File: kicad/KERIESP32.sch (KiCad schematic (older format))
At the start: 30 parts, among them P1 GPIO_0-19, P2 GPIO_21-27, P3 GPIO_32-39, P4 SD_DETECT, P5 USB_Micro_B, P6 GND, P7 Power, SW1 GPIO0, SW2 RESET, U1 ESP-WROOM-32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

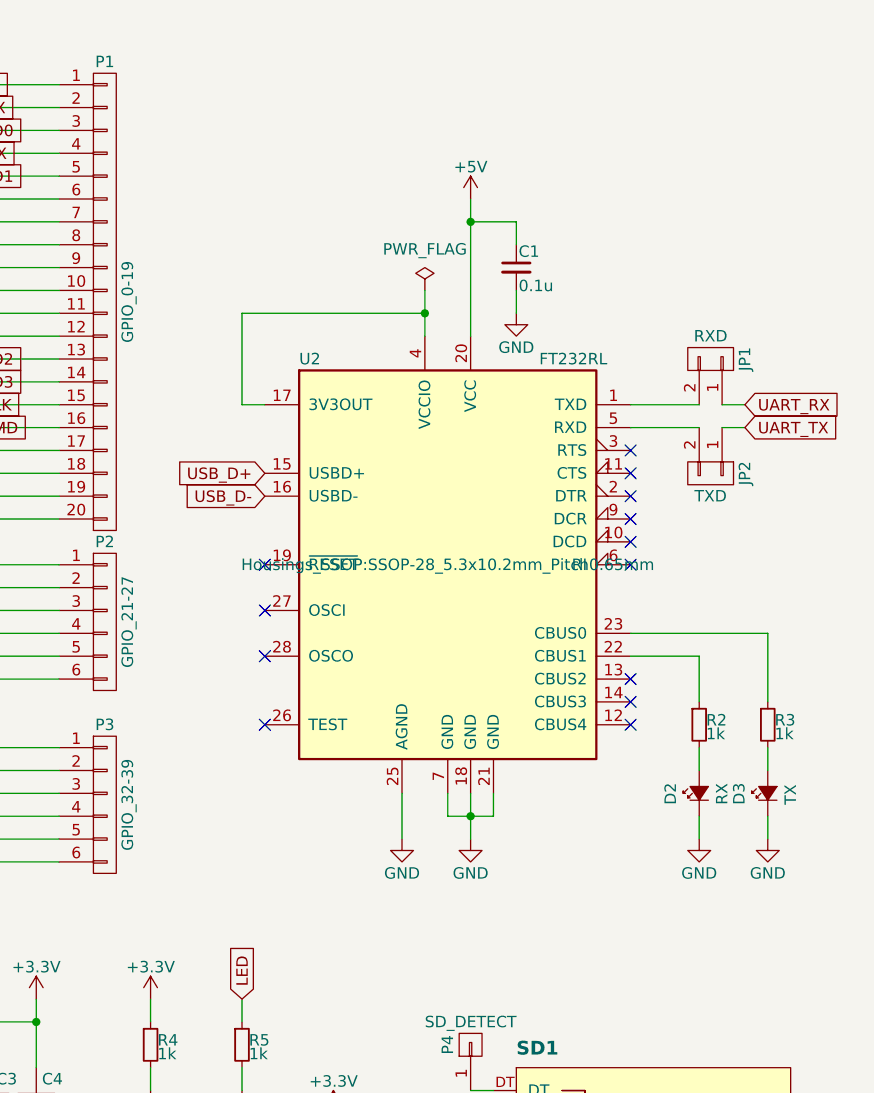
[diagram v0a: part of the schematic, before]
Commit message: 部品表，回路図PDFを生成
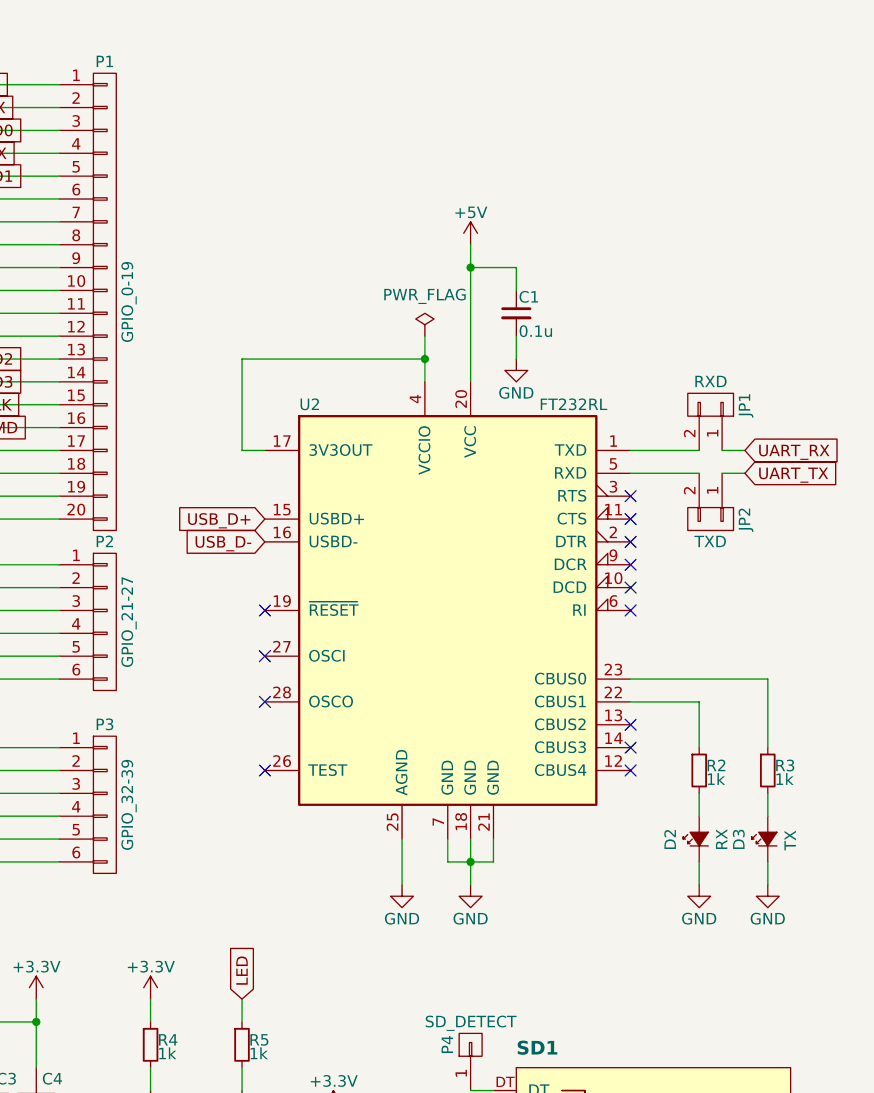
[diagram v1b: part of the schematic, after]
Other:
- moved on the sheet: C1, D2, D3, JP1, JP2, R2, R3, U2

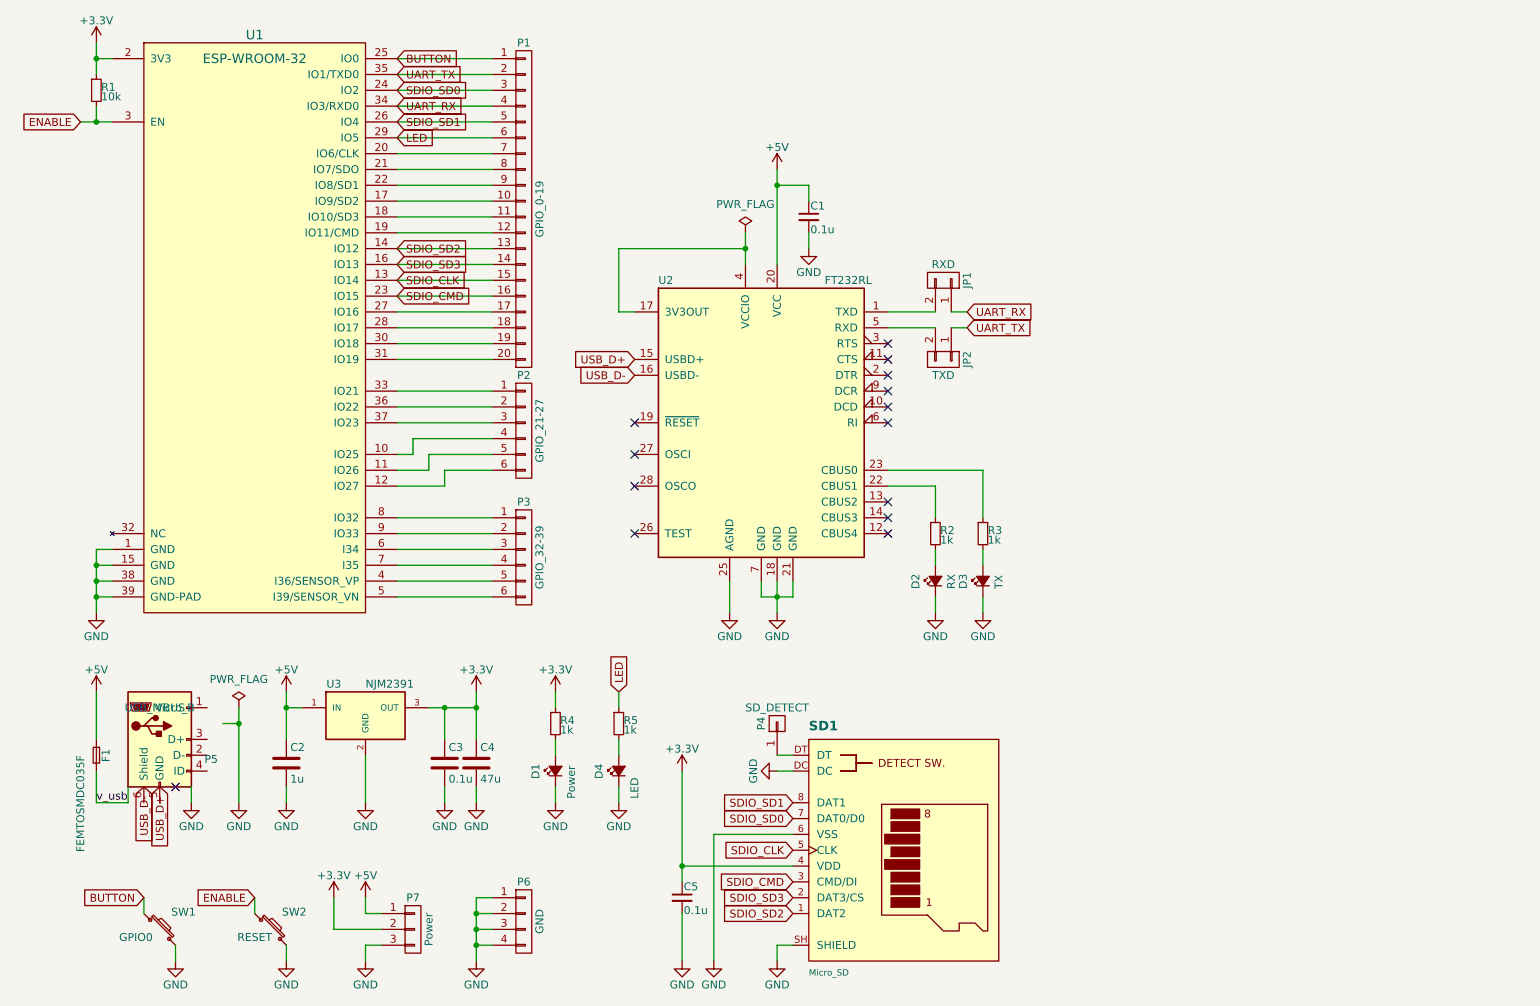
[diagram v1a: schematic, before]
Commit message: 台形型変換基板を設計
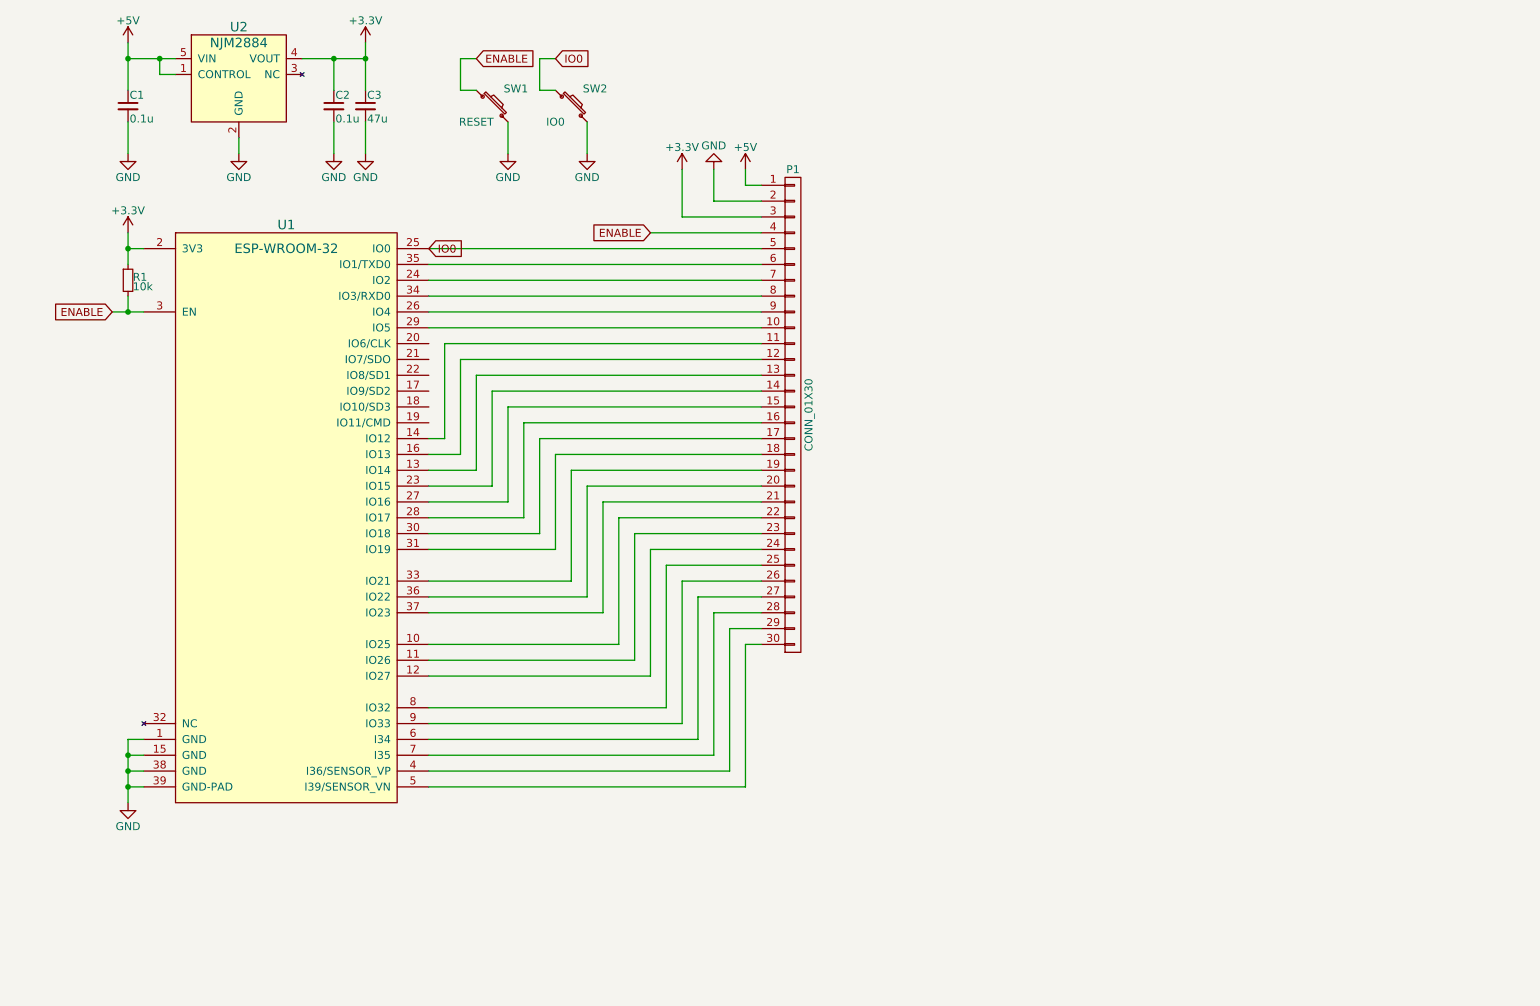
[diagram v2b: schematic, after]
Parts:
- removed C2: 1u, Capacitors_SMD:C_0603, symbol C
- removed C3: 0.1u, Capacitors_SMD:C_0603, symbol C
- removed C4: 47u, Capacitors_SMD:C_1206, symbol C
- removed C5: 0.1u, Capacitors_SMD:C_0603, symbol C_Small
- removed D1: Power, LEDs:LED_0603, symbol Led_Small
- removed D2: RX, LEDs:LED_0603, symbol Led_Small
- removed D3: TX, LEDs:LED_0603, symbol Led_Small
- removed D4: LED, LEDs:LED_0603, symbol Led_Small
- removed F1: FEMTOSMDC035F, Resistors_SMD:R_0603, symbol F_Small
- removed JP1: RXD, Pin_Headers:Pin_Header_Straight_2x01, symbol CONN_01X02
- removed JP2: TXD, Pin_Headers:Pin_Header_Straight_2x01, symbol CONN_01X02
- removed P1: GPIO_0-19, Socket_Strips:Socket_Strip_Straight_1x20, symbol CONN_01X20
- removed P2: GPIO_21-27, Socket_Strips:Socket_Strip_Straight_1x06, symbol CONN_01X06
- removed P3: GPIO_32-39, Socket_Strips:Socket_Strip_Straight_1x06, symbol CONN_01X06
- removed P4: SD_DETECT, Socket_Strips:Socket_Strip_Straight_1x01, symbol CONN_01X01
- removed P5: USB_Micro_B, kerikun11:USB_Micro_B_smd, symbol USB_OTG
- removed P6: GND, Socket_Strips:Socket_Strip_Straight_1x04, symbol CONN_01X04
- removed P7: Power, Socket_Strips:Socket_Strip_Straight_1x03, symbol CONN_01X03
- removed R2, R3, R4, R5: 1k, Resistors_SMD:R_0603, symbol R_Small
- removed SD1: Micro_SD, conn-io:HIROSE-MICROSD-DM3AT-SF, symbol Micro_SD
- removed U2: FT232RL, Housings_SSOP:SSOP-28_5.3x10.2mm_Pitch0.65mm, symbol FT232RL
- removed U3: NJM2391, TO_SOT_Packages_SMD:TO-252-2Lead, symbol LM7805CT
- added C2: 0.1u, Capacitors_SMD:C_0603, symbol C_Small
- added C3: 47u, Capacitors_SMD:C_1206, symbol C_Small
- added P1: CONN_01X30, Pin_Headers:Pin_Header_Straight_1x30, symbol CONN_01X30
- added U2: NJM2884, TO_SOT_Packages_SMD:SOT89-5_Housing, symbol NJM2884
- SW1: value GPIO0 -> RESET; footprint Buttons_Switches_SMD:SW_SPST_KMR2 -> kerikun11:SW_PUSH
- SW2: value RESET -> IO0; footprint Buttons_Switches_SMD:SW_SPST_KMR2 -> kerikun11:SW_PUSH
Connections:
- net +3V3: now also C2.1, C3.1, P1.3 (P3), U2.4 (VOUT)
- net +5V: now also P1.1 (P1), U2.1 (CONTROL), U2.5 (VIN)
- net ENABLE: now also SW1.1, P1.4 (P4); no longer SW2.1
- net GND: now also C2.2, C3.2, P1.2 (P2), U2.2 (GND)
- net at U1.27 (IO16): now also P1.15 (P15)
- net at U1.28 (IO17): now also P1.16 (P16)
- net at U1.30 (IO18): now also P1.17 (P17)
- net at U1.31 (IO19): now also P1.18 (P18)
- net at U1.33 (IO21): now also P1.19 (P19)
- net at U1.36 (IO22): now also P1.20 (P20)
- net at U1.37 (IO23): now also P1.21 (P21)
- net at U1.10 (IO25): now also P1.22 (P22)
- net at U1.11 (IO26): now also P1.23 (P23)
- net at U1.12 (IO27): now also P1.24 (P24)
- net at U1.8 (IO32): now also P1.25 (P25)
- net at U1.9 (IO33): now also P1.26 (P26)
- net at U1.6 (I34): now also P1.27 (P27)
- net at U1.7 (I35): now also P1.28 (P28)
- net at U1.4 (I36/SENSOR_VP): now also P1.29 (P29)
- net at U1.5 (I39/SENSOR_VN): now also P1.30 (P30)
- net BUTTON renamed IO0
- net IO0: now also SW2.1, P1.5 (P5); no longer SW1.1
- net LED: no longer names the net of U1.29 (IO5)
- net LED: now also P1.10 (P10)
- net SDIO_CLK: no longer names the net of U1.13 (IO14)
- net SDIO_CLK: now also P1.13 (P13)
- net SDIO_CMD: no longer names the net of U1.23 (IO15)
- net SDIO_CMD: now also P1.14 (P14)
- net SDIO_SD0: no longer names the net of U1.24 (IO2)
- net SDIO_SD0: now also P1.7 (P7)
- net SDIO_SD1: no longer names the net of U1.26 (IO4)
- net SDIO_SD1: now also P1.9 (P9)
- net SDIO_SD2: no longer names the net of U1.14 (IO12)
- net SDIO_SD2: now also P1.11 (P11)
- net SDIO_SD3: no longer names the net of U1.16 (IO13)
- net SDIO_SD3: now also P1.12 (P12)
- net UART_RX: no longer names the net of U1.34 (IO3/RXD0)
- net UART_RX: now also P1.8 (P8)
- net UART_TX: no longer names the net of U1.35 (IO1/TXD0)
- net UART_TX: now also P1.6 (P6)
- no-connect marks 14 -> 0
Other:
- moved on the sheet: R1, U1

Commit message: 台形基板にSDカードを設置
裏面にMicroSDスロットを取り付け．
形は変わらず
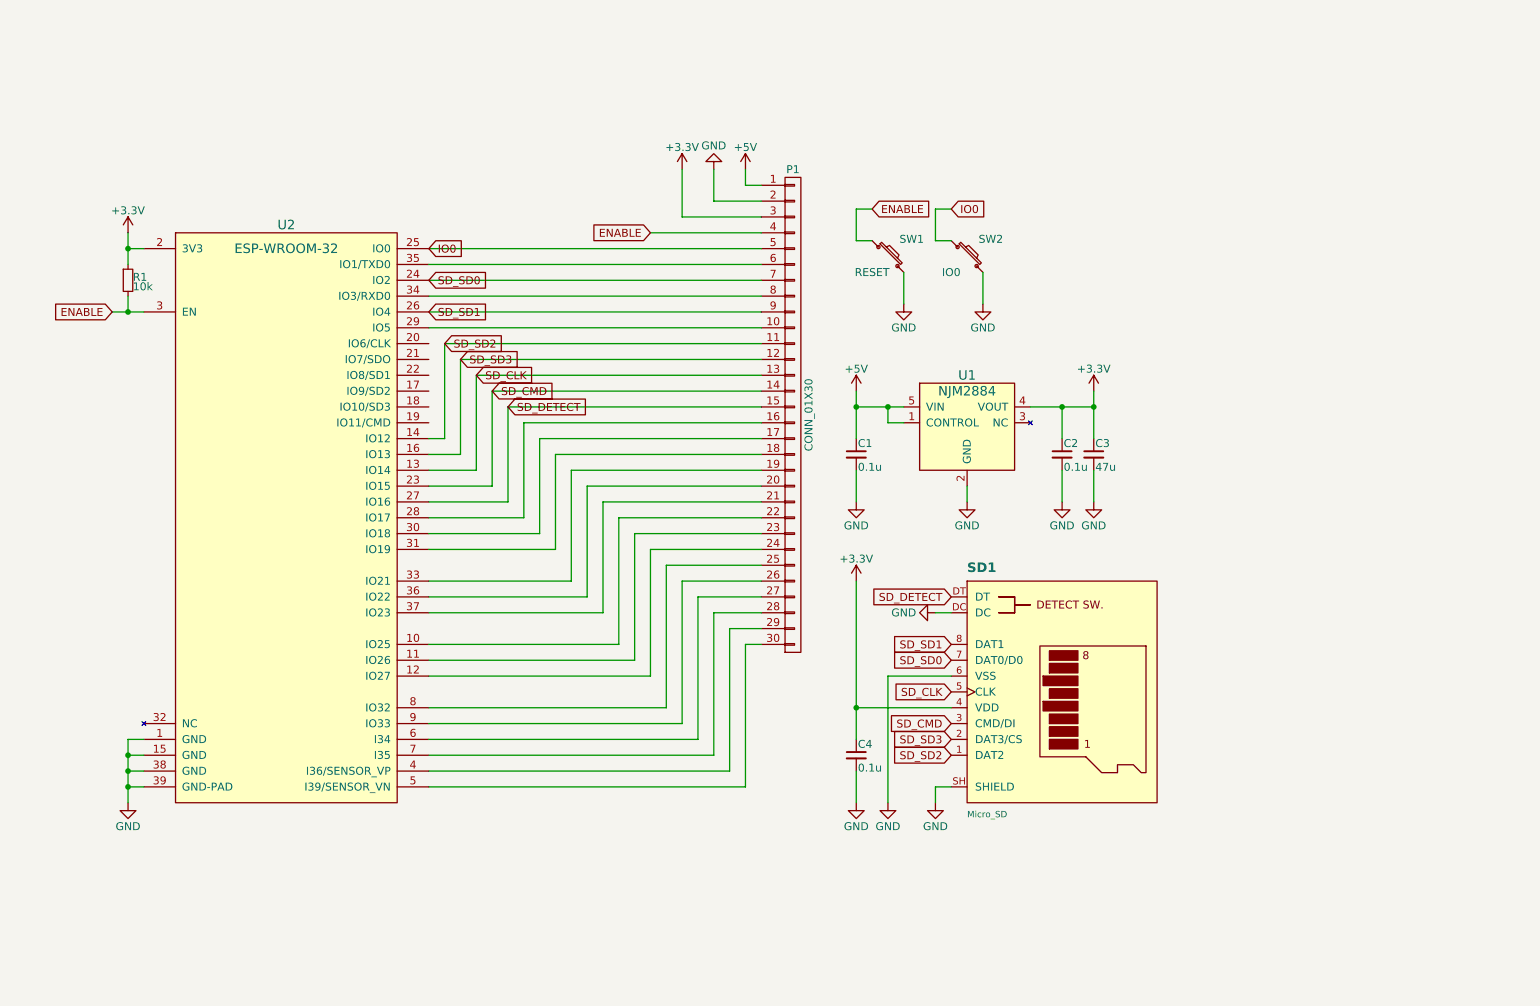
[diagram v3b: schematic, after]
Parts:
- added C4: 0.1u, Capacitors_SMD:C_0603, symbol C_Small
- added SD1: Micro_SD, kerikun11:HIROSE-MICROSD-DM3AT-SF, symbol Micro_SD
- renumbered U2 to U1, U1 to U2
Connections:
- net +3V3: now also C4.1, SD1.4 (VDD)
- net GND: now also C4.2, SD1.6 (VSS), SD1.DC, SD1.SH (SHIELD)
- net SD_CLK: now reaches P1.13 (P13), U2.13 (IO14)
- net SD_CLK: now also SD1.5 (CLK)
- net SD_SD2: now reaches P1.11 (P11), U2.14 (IO12)
- net SD_SD2: now also SD1.1 (DAT2)
- net SD_SD3: now reaches P1.12 (P12), U2.16 (IO13)
- net SD_SD3: now also SD1.2 (DAT3/CS)
- net SD_CMD: now reaches P1.14 (P14), U2.23 (IO15)
- net SD_CMD: now also SD1.3 (CMD/DI)
- net SD_SD0: now reaches P1.7 (P7), U2.24 (IO2)
- net SD_SD0: now also SD1.7 (DAT0/D0)
- net SD_SD1: now reaches P1.9 (P9), U2.26 (IO4)
- net SD_SD1: now also SD1.8 (DAT1)
- net SD_DETECT: now reaches P1.15 (P15), U2.27 (IO16)
- net SD_DETECT: now also SD1.DT
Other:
- moved on the sheet: C1, C2, C3, SW1, SW2, U1

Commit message: ブレッドボード用の基板を設計SIP
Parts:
- added C5, C6: 0.1u, Capacitors_SMD:C_0603, symbol C_Small
- added D1: Power, LEDs:LED_0603, symbol LED
- added F1: FEMTOSMDC035F-02, Capacitors_SMD:C_0603, symbol Polyfuse_Small
- added J1: USB_OTG, KERIESP32:ZX62R-B-5P, symbol USB_OTG
- added R2: 1k, Resistors_SMD:R_0603, symbol R
- added U3: FT231XS, SMD_Packages:SSOP-20, symbol FT231XS
- P1: value CONN_01X30 -> CONN; footprint Pin_Headers:Pin_Header_Straight_1x30 -> Pin_Headers:Pin_Header_Straight_1x30_Pitch2.54mm
- SD1: footprint kerikun11:HIROSE-MICROSD-DM3AT-SF -> KERIESP32:HIROSE-MICROSD-DM3AT-SF
- SW1, SW2: footprint kerikun11:SW_PUSH -> KERIESP32:SW_PUSH
- U1: renamed from U2; footprint kerikun11:ESP-WROOM-32 -> KERIESP32:ESP-WROOM-32
- renumbered C4 to C2, C2 to C3, C3 to C4, U1 to U2
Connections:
- net +3V3: now also D1.2 (A)
- net +5V: now also C6.1, F1.1, U3.15 (VCC)
- net GND: now also C5.2, C6.2, J1.5 (GND), R2.2, U3.16 (GND), U3.6 (GND)
- net RXD: now reaches P1.8 (P8), U1.34 (IO3/RXD0)
- net RXD: now also U3.20 (TXD)
- net TXD: now reaches P1.6 (P6), U1.35 (IO1/TXD0)
- net TXD: now also U3.4 (RXD)
- new net: C5.1, U3.13 (3V3OUT), U3.14 (~RESET), U3.3 (VCCIO)
- new net: D1.1 (K), R2.1
- new net USB_D+: J1.3 (D+), U3.11 (USBDP)
- new net USB_D-: J1.2 (D-), U3.12 (USBDM)
- new net bus: F1.2, J1.1 (VBUS)
- no-connect marks 0 -> 18
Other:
- moved on the sheet: SW1, SW2

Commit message: 小型化，自動配線成功
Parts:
- J1: value USB_OTG -> ZX62R-B-5P
- P1: footprint Pin_Headers:Pin_Header_Straight_1x30_Pitch2.54mm -> KERIESP32:Pin_Header_Straight_1x30_Pitch2.54mm
- SD1: value Micro_SD -> DM3AT-SF-PEJM5
